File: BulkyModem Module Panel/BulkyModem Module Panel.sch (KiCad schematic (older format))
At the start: 15 parts, among them J1 Front Panel, M1 Mounting_Pin, M2 Mounting_Pin, M3 Mounting_Pin, M4 Mounting_Pin, SW1 MODE, SW2 POW

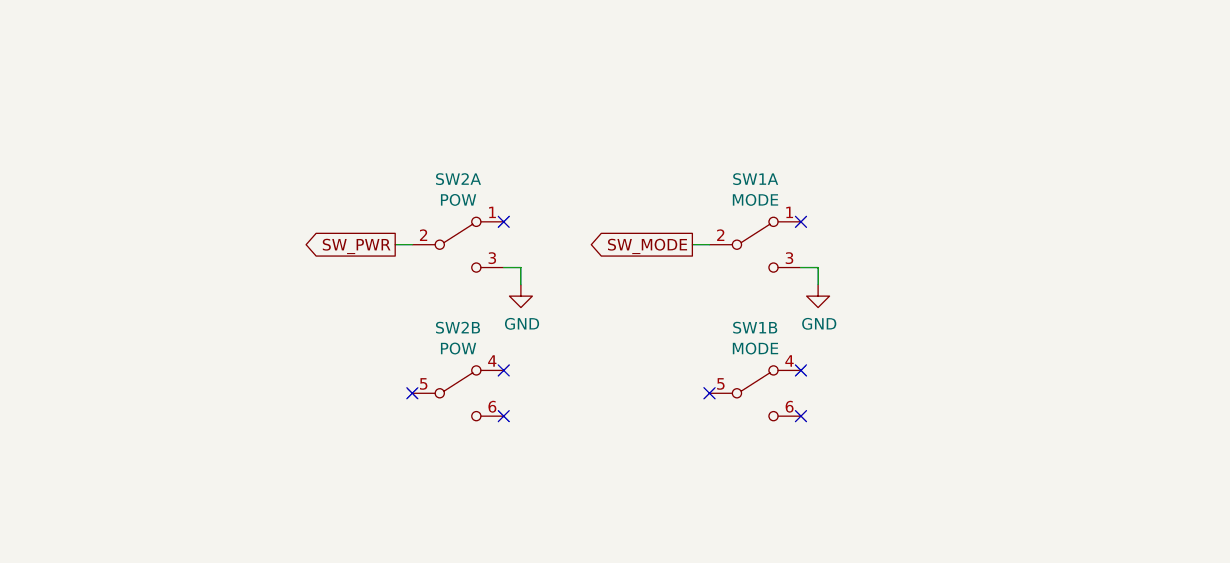
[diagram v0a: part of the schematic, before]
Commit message: Double up power switch
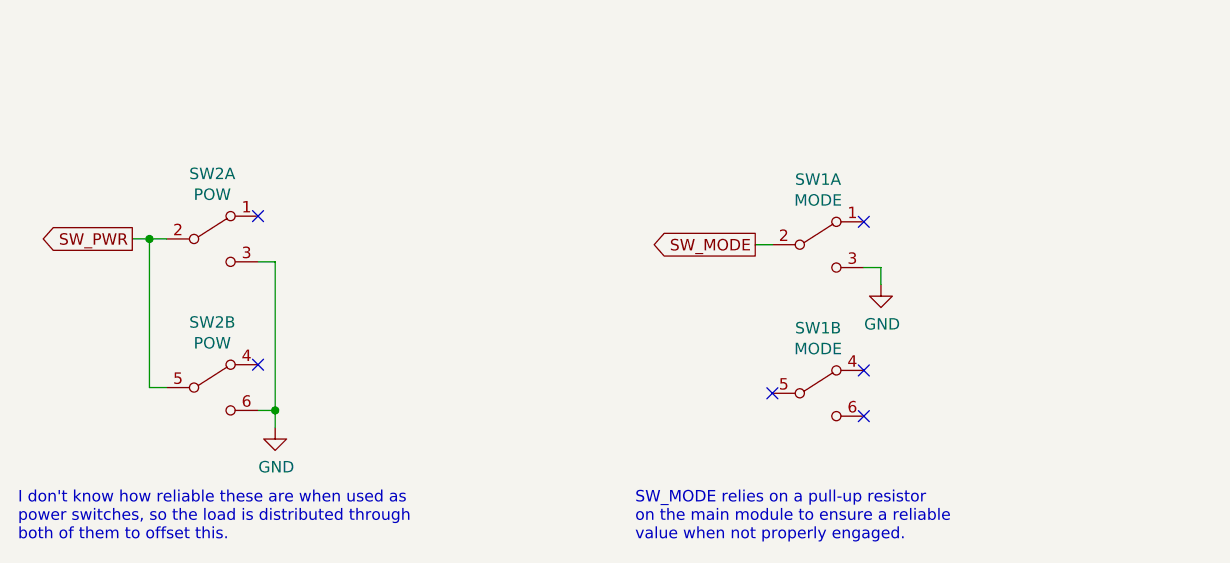
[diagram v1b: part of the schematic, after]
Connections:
- net GND: now also SW2.6 (C)
- net SW_PWR: now also SW2.5 (B)
- no-connect marks 8 -> 6
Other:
- note added: "I don't know how reliable these are when used as\npower switches, so the load is distributed through\nboth of them to offset this."
- note added: "SW_MODE relies on a pull-up resistor\non the main module to ensure a reliable\nvalue when not properly engaged."
- moved on the sheet: SW1A, SW1B, SW2A, SW2B
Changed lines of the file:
@@
 Comment2 ""
 Comment3 ""
-Comment4 "Front panel for mounting LEDs horizontally, designed for slotting into channel board."
+Comment4 "Front panel for mounting LEDs horizontally, designed for slotting into the main module."
 $EndDescr
 $Comp
@@
 L Switch:SW_DPDT_x2 SW1
 U 1 1 62E3B89C
-P 5375 4600
-F 0 "SW1" H 5375 4885 50  0000 C CNN
-F 1 "MODE" H 5375 4794 50  0000 C CNN
-F 2 "6pin_switch:dpdt_switch_black" H 5375 4600 50  0001 C CNN
-F 3 "~" H 5375 4600 50  0001 C CNN
-	1    5375 4600
+P 5650 4600
+F 0 "SW1" H 5650 4885 50  0000 C CNN
+F 1 "MODE" H 5650 4794 50  0000 C CNN
+F 2 "6pin_switch:dpdt_switch_black" H 5650 4600 50  0001 C CNN
+F 3 "~" H 5650 4600 50  0001 C CNN
+	1    5650 4600
 	1    0    0    -1
 $EndComp
@@
 L Switch:SW_DPDT_x2 SW1
 U 2 1 62E3C504
-P 5375 5250
-F 0 "SW1" H 5375 5535 50  0000 C CNN
-F 1 "MODE" H 5375 5444 50  0000 C CNN
-F 2 "6pin_switch:dpdt_switch_black" H 5375 5250 50  0001 C CNN
-F 3 "~" H 5375 5250 50  0001 C CNN
-	2    5375 5250
+P 5650 5250
+F 0 "SW1" H 5650 5535 50  0000 C CNN
+F 1 "MODE" H 5650 5444 50  0000 C CNN
+F 2 "6pin_switch:dpdt_switch_black" H 5650 5250 50  0001 C CNN
+F 3 "~" H 5650 5250 50  0001 C CNN
+	2    5650 5250
 	1    0    0    -1
 $EndComp
@@
 L Switch:SW_DPDT_x2 SW2
 U 1 1 62E3F52F
-P 4075 4600
-F 0 "SW2" H 4075 4885 50  0000 C CNN
-F 1 "POW" H 4075 4794 50  0000 C CNN
-F 2 "6pin_switch:dpdt_switch_black" H 4075 4600 50  0001 C CNN
-F 3 "~" H 4075 4600 50  0001 C CNN
-	1    4075 4600
+P 3000 4575
+F 0 "SW2" H 3000 4860 50  0000 C CNN
+F 1 "POW" H 3000 4769 50  0000 C CNN
+F 2 "6pin_switch:dpdt_switch_black" H 3000 4575 50  0001 C CNN
+F 3 "~" H 3000 4575 50  0001 C CNN
+	1    3000 4575
 	1    0    0    -1
 $EndComp
@@
 L Switch:SW_DPDT_x2 SW2
 U 2 1 62E3FA35
-P 4075 5250
-F 0 "SW2" H 4075 5535 50  0000 C CNN
-F 1 "POW" H 4075 5444 50  0000 C CNN
-F 2 "6pin_switch:dpdt_switch_black" H 4075 5250 50  0001 C CNN
-F 3 "~" H 4075 5250 50  0001 C CNN
-	2    4075 5250
+P 3000 5225
+F 0 "SW2" H 3000 5510 50  0000 C CNN
+F 1 "POW" H 3000 5419 50  0000 C CNN
+F 2 "6pin_switch:dpdt_switch_black" H 3000 5225 50  0001 C CNN
+F 3 "~" H 3000 5225 50  0001 C CNN
+	2    3000 5225
 	1    0    0    -1
 $EndComp
@@
 	0    -1   -1   0
 $EndComp
-Text GLabel 3800 4600 0    50   Output ~ 0
+Text GLabel 2650 4575 0    50   Output ~ 0
 SW_PWR
-Wire Wire Line
-	3800 4600 3875 4600
-NoConn ~ 4275 4500
+NoConn ~ 3200 4475
 $Comp
 L power:GND #PWR0112
 U 1 1 62E61DCC
-P 4350 4775
-F 0 "#PWR0112" H 4350 4525 50  0001 C CNN
-F 1 "GND" H 4355 4602 50  0000 C CNN
-F 2 "" H 4350 4775 50  0001 C CNN
-F 3 "" H 4350 4775 50  0001 C CNN
-	1    4350 4775
-	1    0    0    -1
-$EndComp
-Wire Wire Line
-	4275 4700 4350 4700
-Wire Wire Line
-	4350 4700 4350 4775
-NoConn ~ 4275 5150
-Text GLabel 5100 4600 0    50   Output ~ 0
+P 3275 5400
+F 0 "#PWR0112" H 3275 5150 50  0001 C CNN
+F 1 "GND" H 3280 5227 50  0000 C CNN
+F 2 "" H 3275 5400 50  0001 C CNN
+F 3 "" H 3275 5400 50  0001 C CNN
+	1    3275 5400
+	1    0    0    -1
+$EndComp
+Wire Wire Line
+	3200 5325 3275 5325
+Wire Wire Line
+	3275 5325 3275 5400
+NoConn ~ 3200 5125
+Text GLabel 5375 4600 0    50   Output ~ 0
 SW_MODE
 Wire Wire Line
-	5100 4600 5175 4600
-NoConn ~ 5575 4500
+	5375 4600 5450 4600
+NoConn ~ 5850 4500
 $Comp
 L power:GND #PWR0113
 U 1 1 62E7FC92
-P 5650 4775
-F 0 "#PWR0113" H 5650 4525 50  0001 C CNN
-F 1 "GND" H 5655 4602 50  0000 C CNN
-F 2 "" H 5650 4775 50  0001 C CNN
-F 3 "" H 5650 4775 50  0001 C CNN
-	1    5650 4775
-	1    0    0    -1
-$EndComp
-Wire Wire Line
-	5575 4700 5650 4700
-Wire Wire Line
-	5650 4700 5650 4775
-NoConn ~ 5175 5250
-NoConn ~ 5575 5150
-NoConn ~ 5575 5350
-NoConn ~ 3875 5250
-NoConn ~ 4275 5350
+P 5925 4775
+F 0 "#PWR0113" H 5925 4525 50  0001 C CNN
+F 1 "GND" H 5930 4602 50  0000 C CNN
+F 2 "" H 5925 4775 50  0001 C CNN
+F 3 "" H 5925 4775 50  0001 C CNN
+	1    5925 4775
+	1    0    0    -1
+$EndComp
+Wire Wire Line
+	5850 4700 5925 4700
+Wire Wire Line
+	5925 4700 5925 4775
+NoConn ~ 5450 5250
+NoConn ~ 5850 5150
+NoConn ~ 5850 5350
+Text Notes 4850 5900 0    50   ~ 0
+SW_MODE relies on a pull-up resistor\non the main module to ensure a reliable\nvalue when not properly engaged.
+Wire Wire Line
+	2650 4575 2725 4575
+Wire Wire Line
+	2725 4575 2725 5225
+Wire Wire Line
+	2725 5225 2800 5225
+Connection ~ 2725 4575
+Wire Wire Line
+	2725 4575 2800 4575
+Wire Wire Line
+	3275 5325 3275 4675
+Wire Wire Line
+	3275 4675 3200 4675
+Connection ~ 3275 5325
+Text Notes 2150 5900 0    50   ~ 0
+I don't know how reliable these are when used as\npower switches, so the load is distributed through\nboth of them to offset this.
 Wire Bus Line
 	8275 2725 8275 3425

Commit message: Add DCD
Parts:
- added D1: DCD, LED_THT:LED_D5.0mm, symbol Device:LED
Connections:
- net LED_C64: now also J1.11 (RS-232); no longer J1.10 (RI)
- net LED_CTS: now also J1.8 (CTS); no longer J1.7 (RTS)
- net LED_RS232: now also J1.10 (RI); no longer J1.9 (DCD)
- net LED_RTS: now also J1.7 (RTS); no longer J1.8 (CTS)
- net LED_RX: now also J1.6 (RX); no longer J1.5 (TX)
- net LED_TX: now also J1.5 (TX); no longer J1.6 (RX)
- net VCC: now also D1.2 (A)
- new net LED_DCD: D1.1 (K), J1.9 (DCD)
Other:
- moved on the sheet: D10, D11, D12, D13, D14, D15
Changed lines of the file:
@@
 Text Label 8400 2725 0    50   ~ 0
 LED_DATA
+Text Label 8400 2925 0    50   ~ 0
+LED_RX
 Text Label 8400 2825 0    50   ~ 0
-LED_RX
-Text Label 8400 2925 0    50   ~ 0
 LED_TX
+Text Label 8400 3125 0    50   ~ 0
+LED_CTS
 Text Label 8400 3025 0    50   ~ 0
-LED_CTS
-Text Label 8400 3125 0    50   ~ 0
 LED_RTS
-Text Label 8400 3225 0    50   ~ 0
+Text Label 8400 3325 0    50   ~ 0
 LED_RS232
-Text Label 8400 3325 0    50   ~ 0
+Text Label 8400 3425 0    50   ~ 0
 LED_C64
 Entry Wire Line
@@
 	8375 3125 8275 3225
 Entry Wire Line
-	8375 3225 8275 3325
-Entry Wire Line
 	8375 3325 8275 3425
+Entry Wire Line
+	8375 3425 8275 3525
 $Comp
 L power:PWR_FLAG #FLG0101
@@
 	8850 4425 9025 4425
 Entry Wire Line
-	4900 3425 4800 3325
+	4500 3425 4400 3325
 $Comp
 L Device:LED D10
 U 1 1 62876713
+P 4400 2700
+F 0 "D10" V 4439 2582 50  0000 R CNN
+F 1 "C64" V 4348 2582 50  0000 R CNN
+F 2 "LED_THT:LED_D5.0mm" H 4400 2700 50  0001 C CNN
+F 3 "~" H 4400 2700 50  0001 C CNN
+	1    4400 2700
+	0    -1   -1   0
+$EndComp
+$Comp
+L power:VCC #PWR0103
+U 1 1 62876719
+P 4400 2550
+F 0 "#PWR0103" H 4400 2400 50  0001 C CNN
+F 1 "VCC" H 4415 2723 50  0000 C CNN
+F 2 "" H 4400 2550 50  0001 C CNN
+F 3 "" H 4400 2550 50  0001 C CNN
+	1    4400 2550
+	1    0    0    -1
+$EndComp
+Entry Wire Line
+	4900 3425 4800 3325
+$Comp
+L Device:LED D11
+U 1 1 62876721
 P 4800 2700
-F 0 "D10" V 4839 2582 50  0000 R CNN
-F 1 "C64" V 4748 2582 50  0000 R CNN
+F 0 "D11" V 4839 2582 50  0000 R CNN
+F 1 "RS-232" V 4748 2582 50  0000 R CNN
 F 2 "LED_THT:LED_D5.0mm" H 4800 2700 50  0001 C CNN
 F 3 "~" H 4800 2700 50  0001 C CNN
@@
 $EndComp
 $Comp
-L power:VCC #PWR0103
-U 1 1 62876719
+L power:VCC #PWR0104
+U 1 1 62876727
 P 4800 2550
-F 0 "#PWR0103" H 4800 2400 50  0001 C CNN
+F 0 "#PWR0104" H 4800 2400 50  0001 C CNN
 F 1 "VCC" H 4815 2723 50  0000 C CNN
 F 2 "" H 4800 2550 50  0001 C CNN
@@
 $EndComp
 Entry Wire Line
-	5300 3425 5200 3325
-$Comp
-L Device:LED D11
-U 1 1 62876721
-P 5200 2700
-F 0 "D11" V 5239 2582 50  0000 R CNN
-F 1 "RS-232" V 5148 2582 50  0000 R CNN
-F 2 "LED_THT:LED_D5.0mm" H 5200 2700 50  0001 C CNN
-F 3 "~" H 5200 2700 50  0001 C CNN
-	1    5200 2700
-	0    -1   -1   0
-$EndComp
-$Comp
-L power:VCC #PWR0104
-U 1 1 62876727
-P 5200 2550
-F 0 "#PWR0104" H 5200 2400 50  0001 C CNN
-F 1 "VCC" H 5215 2723 50  0000 C CNN
-F 2 "" H 5200 2550 50  0001 C CNN
-F 3 "" H 5200 2550 50  0001 C CNN
-	1    5200 2550
-	1    0    0    -1
-$EndComp
-Entry Wire Line
-	5850 3425 5750 3325
+	6250 3425 6150 3325
 $Comp
 L power:VCC #PWR0105
 U 1 1 62876735
+P 6150 2550
+F 0 "#PWR0105" H 6150 2400 50  0001 C CNN
+F 1 "VCC" H 6165 2723 50  0000 C CNN
+F 2 "" H 6150 2550 50  0001 C CNN
+F 3 "" H 6150 2550 50  0001 C CNN
+	1    6150 2550
+	1    0    0    -1
+$EndComp
+Entry Wire Line
+	5850 3425 5750 3325
+$Comp
+L Device:LED D13
+U 1 1 6287673D
+P 5750 2700
+F 0 "D13" V 5789 2582 50  0000 R CNN
+F 1 "CTS" V 5698 2582 50  0000 R CNN
+F 2 "LED_THT:LED_D5.0mm" H 5750 2700 50  0001 C CNN
+F 3 "~" H 5750 2700 50  0001 C CNN
+	1    5750 2700
+	0    -1   -1   0
+$EndComp
+$Comp
+L power:VCC #PWR0106
+U 1 1 62876743
 P 5750 2550
-F 0 "#PWR0105" H 5750 2400 50  0001 C CNN
+F 0 "#PWR0106" H 5750 2400 50  0001 C CNN
 F 1 "VCC" H 5765 2723 50  0000 C CNN
 F 2 "" H 5750 2550 50  0001 C CNN
@@
 $EndComp
 Entry Wire Line
-	6250 3425 6150 3325
-$Comp
-L Device:LED D13
-U 1 1 6287673D
-P 6150 2700
-F 0 "D13" V 6189 2582 50  0000 R CNN
-F 1 "CTS" V 6098 2582 50  0000 R CNN
-F 2 "LED_THT:LED_D5.0mm" H 6150 2700 50  0001 C CNN
-F 3 "~" H 6150 2700 50  0001 C CNN
-	1    6150 2700
-	0    -1   -1   0
-$EndComp
-$Comp
-L power:VCC #PWR0106
-U 1 1 62876743
-P 6150 2550
-F 0 "#PWR0106" H 6150 2400 50  0001 C CNN
-F 1 "VCC" H 6165 2723 50  0000 C CNN
-F 2 "" H 6150 2550 50  0001 C CNN
-F 3 "" H 6150 2550 50  0001 C CNN
-	1    6150 2550
-	1    0    0    -1
-$EndComp
-Entry Wire Line
-	6650 3425 6550 3325
+	7050 3425 6950 3325
 $Comp
 L Device:LED D14
 U 1 1 6287674B
+P 6950 2700
+F 0 "D14" V 6989 2582 50  0000 R CNN
+F 1 "TX" V 6898 2582 50  0000 R CNN
+F 2 "LED_THT:LED_D5.0mm" H 6950 2700 50  0001 C CNN
+F 3 "~" H 6950 2700 50  0001 C CNN
+	1    6950 2700
+	0    -1   -1   0
+$EndComp
+$Comp
+L power:VCC #PWR0107
+U 1 1 62876751
+P 6950 2550
+F 0 "#PWR0107" H 6950 2400 50  0001 C CNN
+F 1 "VCC" H 6965 2723 50  0000 C CNN
+F 2 "" H 6950 2550 50  0001 C CNN
+F 3 "" H 6950 2550 50  0001 C CNN
+	1    6950 2550
+	1    0    0    -1
+$EndComp
+Entry Wire Line
+	6650 3425 6550 3325
+$Comp
+L Device:LED D15
+U 1 1 62876759
 P 6550 2700
-F 0 "D14" V 6589 2582 50  0000 R CNN
-F 1 "TX" V 6498 2582 50  0000 R CNN
+F 0 "D15" V 6589 2582 50  0000 R CNN
+F 1 "RX" V 6498 2582 50  0000 R CNN
 F 2 "LED_THT:LED_D5.0mm" H 6550 2700 50  0001 C CNN
 F 3 "~" H 6550 2700 50  0001 C CNN
@@
 $EndComp
 $Comp
-L power:VCC #PWR0107
-U 1 1 62876751
+L power:VCC #PWR0108
+U 1 1 6287675F
 P 6550 2550
-F 0 "#PWR0107" H 6550 2400 50  0001 C CNN
+F 0 "#PWR0108" H 6550 2400 50  0001 C CNN
 F 1 "VCC" H 6565 2723 50  0000 C CNN
 F 2 "" H 6550 2550 50  0001 C CNN
 F 3 "" H 6550 2550 50  0001 C CNN
 	1    6550 2550
-	1    0    0    -1
-$EndComp
-Entry Wire Line
-	7050 3425 6950 3325
-$Comp
-L Device:LED D15
-U 1 1 62876759
-P 6950 2700
-F 0 "D15" V 6989 2582 50  0000 R CNN
-F 1 "RX" V 6898 2582 50  0000 R CNN
-F 2 "LED_THT:LED_D5.0mm" H 6950 2700 50  0001 C CNN
-F 3 "~" H 6950 2700 50  0001 C CNN
-	1    6950 2700
-	0    -1   -1   0
-$EndComp
-$Comp
-L power:VCC #PWR0108
-U 1 1 6287675F
-P 6950 2550
-F 0 "#PWR0108" H 6950 2400 50  0001 C CNN
-F 1 "VCC" H 6965 2723 50  0000 C CNN
-F 2 "" H 6950 2550 50  0001 C CNN
-F 3 "" H 6950 2550 50  0001 C CNN
-	1    6950 2550
 	1    0    0    -1
 $EndComp
@@
 	8375 3125 9025 3125
 Wire Wire Line
-	8375 3225 9025 3225
-Wire Wire Line
 	8375 3325 9025 3325
+Wire Wire Line
+	8375 3425 9025 3425
 Wire Wire Line
 	8775 4125 9025 4125
@@
 Text Label 7350 3300 1    50   ~ 0
 LED_DATA
+Text Label 6550 3300 1    50   ~ 0
+LED_RX
 Text Label 6950 3300 1    50   ~ 0
-LED_RX
-Text Label 6550 3300 1    50   ~ 0
 LED_TX
+Text Label 5750 3300 1    50   ~ 0
+LED_CTS
 Text Label 6150 3300 1    50   ~ 0
-LED_CTS
-Text Label 5750 3300 1    50   ~ 0
 LED_RTS
-Text Label 5200 3300 1    50   ~ 0
+Text Label 4800 3300 1    50   ~ 0
 LED_RS232
-Text Label 4800 3300 1    50   ~ 0
+Text Label 4400 3300 1    50   ~ 0
 LED_C64
 Wire Wire Line
+	4400 2850 4400 3325
+Wire Wire Line
 	4800 2850 4800 3325
 Wire Wire Line
-	5200 2850 5200 3325
-Wire Wire Line
-	5750 2850 5750 3325
-Wire Wire Line
-	6150 3325 6150 2850
-Wire Wire Line
-	6550 2850 6550 3325
-Wire Wire Line
-	6950 3325 6950 2850
+	6150 2850 6150 3325
+Wire Wire Line
+	5750 3325 5750 2850
+Wire Wire Line
+	6950 2850 6950 3325
+Wire Wire Line
+	6550 3325 6550 2850
 Wire Wire Line
 	7350 2850 7350 3325
@@
 L Device:LED D12
 U 1 1 6287672F
-P 5750 2700
-F 0 "D12" V 5789 2582 50  0000 R CNN
-F 1 "RTS" V 5698 2582 50  0000 R CNN
-F 2 "LED_THT:LED_D5.0mm" H 5750 2700 50  0001 C CNN
-F 3 "~" H 5750 2700 50  0001 C CNN
-	1    5750 2700
+P 6150 2700
+F 0 "D12" V 6189 2582 50  0000 R CNN
+F 1 "RTS" V 6098 2582 50  0000 R CNN
+F 2 "LED_THT:LED_D5.0mm" H 6150 2700 50  0001 C CNN
+F 3 "~" H 6150 2700 50  0001 C CNN
+	1    6150 2700
 	0    -1   -1   0
 $EndComp
@@
 Text Notes 2150 5900 0    50   ~ 0
 I don't know how reliable these are when used as\npower switches, so the load is distributed through\nboth of them to offset this.
+Text Label 8400 3225 0    50   ~ 0
+LED_DCD
+Entry Wire Line
+	8375 3225 8275 3325
+Wire Wire Line
+	8375 3225 9025 3225
+Entry Wire Line
+	5450 3425 5350 3325
+$Comp
+L Device:LED D1
+U 1 1 62E0C4F3
+P 5350 2700
+F 0 "D1" V 5389 2582 50  0000 R CNN
+F 1 "DCD" V 5298 2582 50  0000 R CNN
+F 2 "LED_THT:LED_D5.0mm" H 5350 2700 50  0001 C CNN
+F 3 "~" H 5350 2700 50  0001 C CNN
+	1    5350 2700
+	0    -1   -1   0
+$EndComp
+$Comp
+L power:VCC #PWR01
+U 1 1 62E0C4F9
+P 5350 2550
+F 0 "#PWR01" H 5350 2400 50  0001 C CNN
+F 1 "VCC" H 5365 2723 50  0000 C CNN
+F 2 "" H 5350 2550 50  0001 C CNN
+F 3 "" H 5350 2550 50  0001 C CNN
+	1    5350 2550
+	1    0    0    -1
+$EndComp
+Text Label 5350 3300 1    50   ~ 0
+LED_DCD
+Wire Wire Line
+	5350 3325 5350 2850
 Wire Bus Line
-	8275 2725 8275 3425
+	4500 3425 8075 3425
 Wire Bus Line
-	4900 3425 8075 3425
+	8275 2725 8275 3525
 $EndSCHEMATC
